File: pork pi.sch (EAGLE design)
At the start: 280 parts, among them J1 SJ-2523-SMT-TR, J3 MICRO-SD, J4 POWER_JACKPTH, J5 HDMI-SMD, J6 RB1-125BAG1A, J7 USB+SHIELD-MICROB, J8 USB-STACKED, J9 USB-STACKED, Q1 DMP3098L-7, U1 A13, U10 ENC28J60-QFN, U11 NAND, U12 TUSB2077, U13 HC-05-EZ, U14 TPS2042, U15 TPS2042, U16 TPS2042, U19 IP4220CZ6, U2 AXP209, U20 IP4220CZ6, U21 IP4220CZ6, U3 AP2161DM8G-13, U4 HC-05, U5 MIC2250YML, U6 AP3409DNTR-G1, U7 AP3409DNTR-G1, U8 ST1S10PUR, U9 TFP410, Y1 24MHz, Y2 25MHz, Y3 6MHz

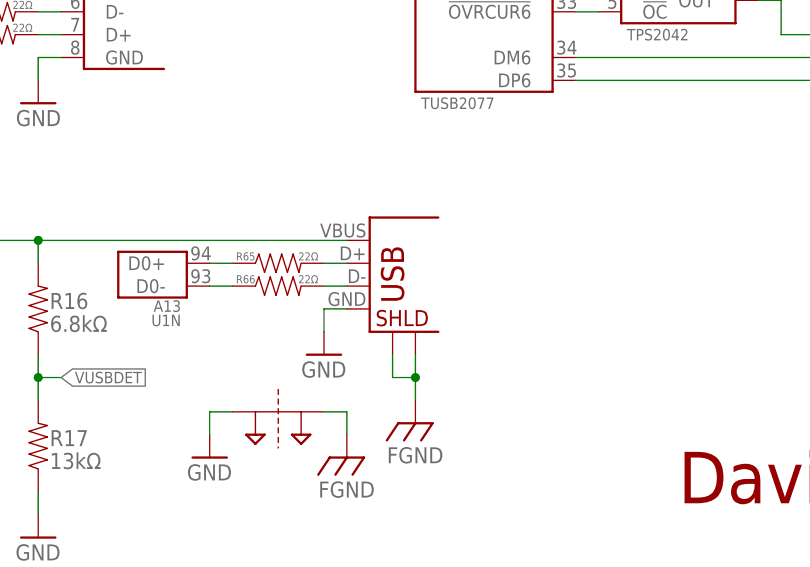
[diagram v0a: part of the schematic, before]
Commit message: Schematic update
Updated the HDMI differential pair names in schematic
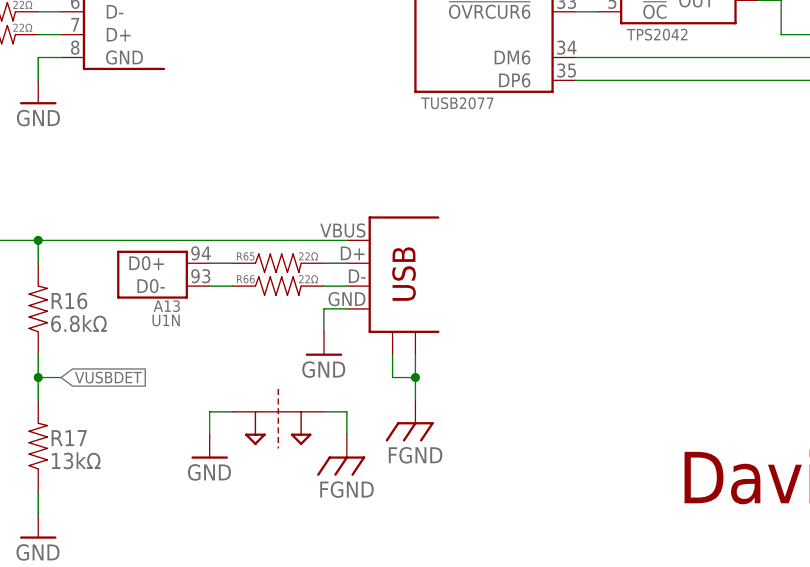
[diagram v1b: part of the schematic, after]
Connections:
- net N$130 renamed T2_P
- net N$131 renamed T2_N
- net N$132 renamed T1_P
- net N$133 renamed T1_N
- net N$134 renamed T0_P
- net N$135 renamed T0_N
- net N$136 renamed TC_P
- net N$137 renamed TC_N
- net FGND: now also J7.S1, J7.S2; no longer J7.P$1, J7.P$2
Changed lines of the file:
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@@
 <segment>
 <pinref part="FGND13" gate="G$1" pin="FGND"/>
-<pinref part="J7" gate="G$1" pin="P$2"/>
+<pinref part="J7" gate="G$1" pin="S2"/>
 <wire x1="154.94" y1="-795.02" x2="154.94" y2="-792.48" width="0.1524" layer="91"/>
-<pinref part="J7" gate="G$1" pin="P$1"/>
+<pinref part="J7" gate="G$1" pin="S1"/>
 <wire x1="154.94" y1="-792.48" x2="154.94" y2="-789.94" width="0.1524" layer="91"/>
 <wire x1="154.94" y1="-792.48" x2="152.4" y2="-792.48" width="0.1524" layer="91"/>
@@
 </segment>
 </net>
-<net name="N$130" class="0">
+<net name="T2_P" class="0">
 <segment>
 <pinref part="U9" gate="B" pin="TX2+"/>
@@
 </segment>
 </net>
-<net name="N$131" class="0">
+<net name="T2_N" class="0">
 <segment>
 <pinref part="J5" gate="G$1" pin="TX2-"/>
@@
 </segment>
 </net>
-<net name="N$132" class="0">
+<net name="T1_P" class="0">
 <segment>
 <pinref part="U9" gate="B" pin="TX1+"/>
@@
 </segment>
 </net>
-<net name="N$133" class="0">
+<net name="T1_N" class="0">
 <segment>
 <pinref part="J5" gate="G$1" pin="TX1-"/>
@@
 </segment>
 </net>
-<net name="N$134" class="0">
+<net name="T0_P" class="0">
 <segment>
 <pinref part="U9" gate="B" pin="TX0+"/>
@@
 </segment>
 </net>
-<net name="N$135" class="0">
+<net name="T0_N" class="0">
 <segment>
 <pinref part="J5" gate="G$1" pin="TX0-"/>
@@
 </segment>
 </net>
-<net name="N$136" class="0">
+<net name="TC_P" class="0">
 <segment>
 <pinref part="U9" gate="B" pin="TXC+"/>
@@
 </segment>
 </net>
-<net name="N$137" class="0">
+<net name="TC_N" class="0">
 <segment>
 <pinref part="J5" gate="G$1" pin="TXC-"/>
